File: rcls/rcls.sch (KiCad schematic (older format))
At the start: 9 parts

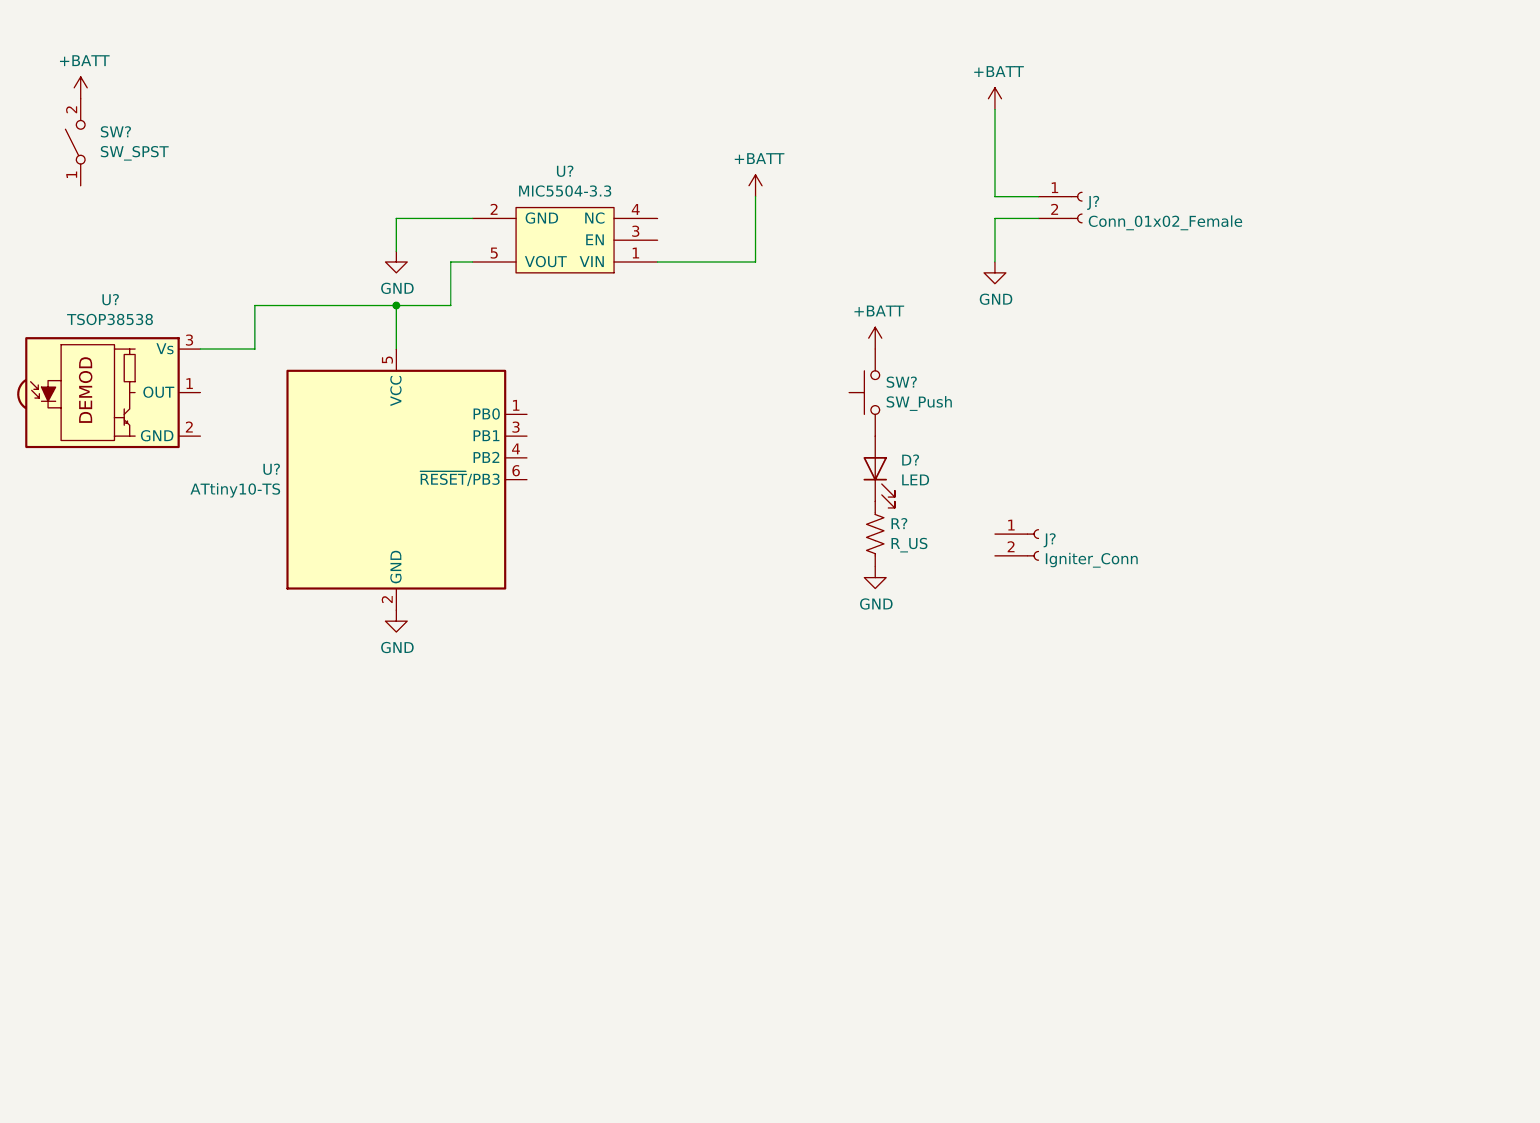
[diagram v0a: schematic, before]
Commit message: Finish initial schematic.
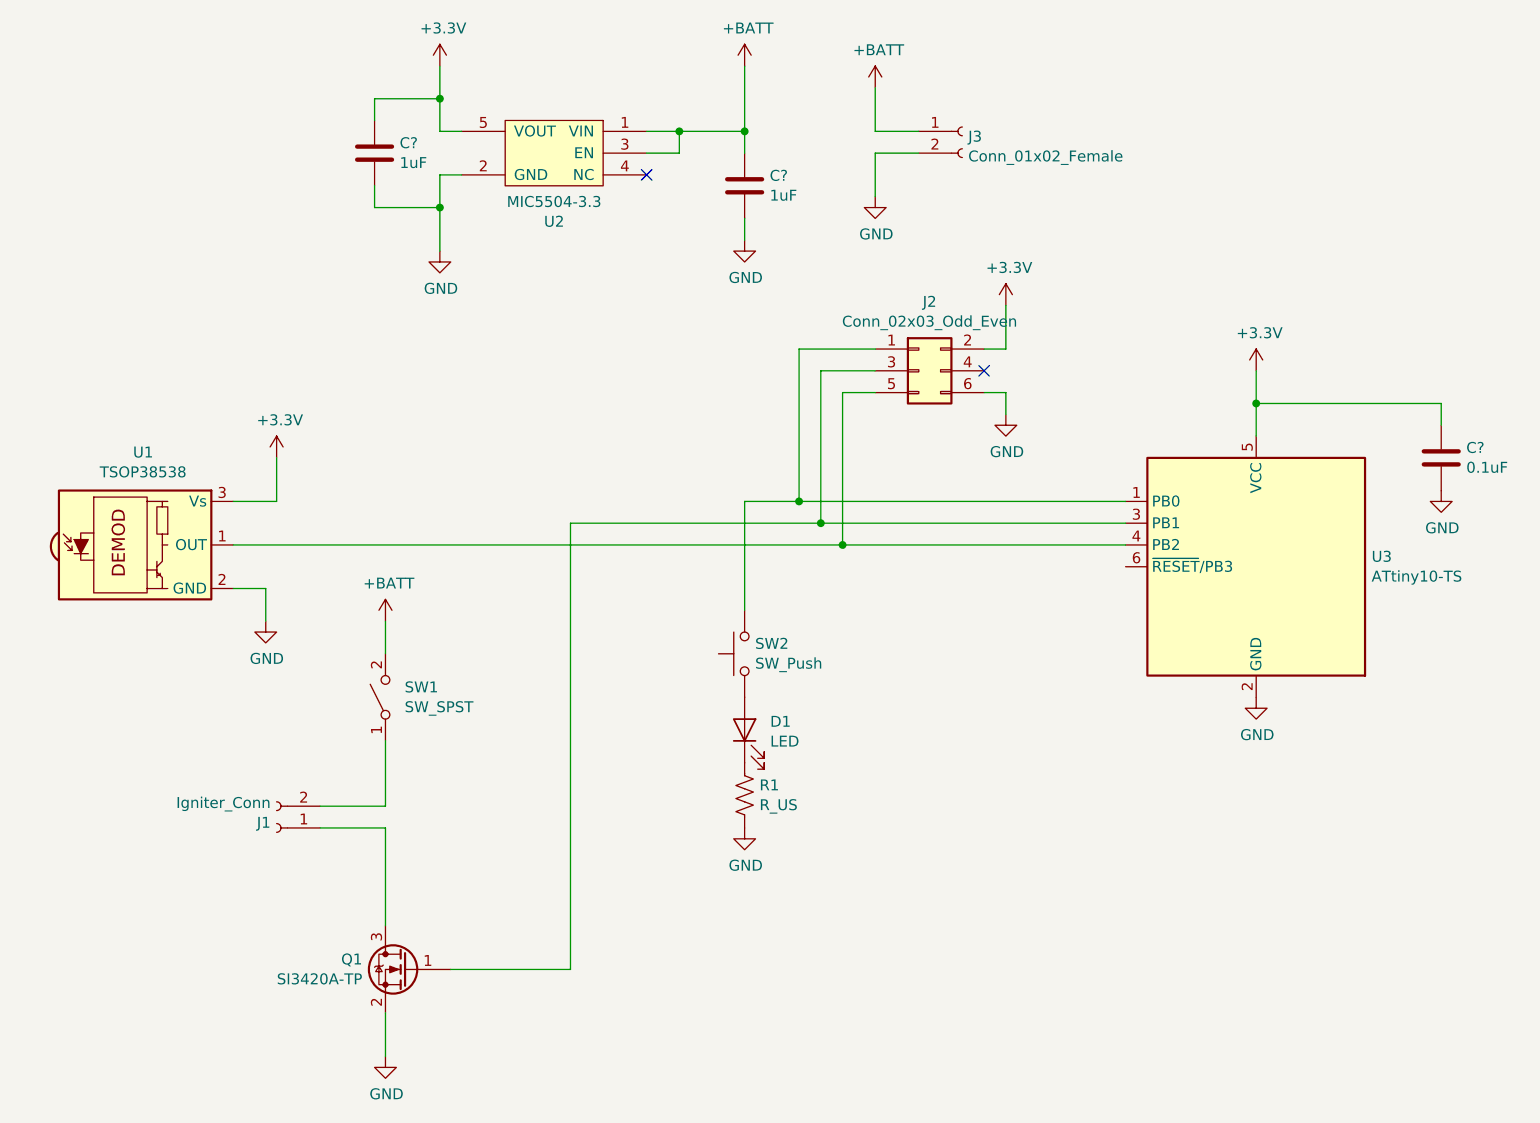
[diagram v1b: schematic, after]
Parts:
- added C? (x2): 1uF, symbol Device:C
- added C?: 0.1uF, symbol Device:C
- added J2: Conn_02x03_Odd_Even, symbol Connector_Generic:Conn_02x03_Odd_Even
- added Q1: SI3420A-TP, Package_TO_SOT_SMD:SOT-23, symbol Transistor_FET:BSS138
- gave numbers to parts that had none: 9
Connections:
- net +BATT: now also U2.3 (EN), C?.1; no longer SW2.2
- net GND: now also U1.2 (GND), C?.2, C?.2, C?.2, J2.6 (Pin_6), Q1.2 (S)
- net at J1.1 (Pin_1): now also Q1.3 (D)
- net at J1.2 (Pin_2): now also SW1.1 (A)
- net at U1.1 (OUT): now also U3.4 (PB2), J2.5 (Pin_5)
- net +3V3: now reaches U1.3 (Vs), U2.5 (VOUT), U3.5 (VCC)
- net +3V3: now also C?.1, C?.1, J2.2 (Pin_2)
- net at U3.1 (PB0): now also SW2.2, J2.1 (Pin_1)
- net at U3.3 (PB1): now also J2.3 (Pin_3), Q1.1 (G)
- no-connect marks 0 -> 2
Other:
- moved on the sheet: D1, J1, J3, R1, SW1, SW2, U1, U2, U3
